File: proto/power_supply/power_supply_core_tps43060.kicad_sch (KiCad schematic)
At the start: 45 parts, among them Q201 TK4R3E06PL, Q202 TK4R3E06PL, U101 ZXCT1110, U202 TPS43060

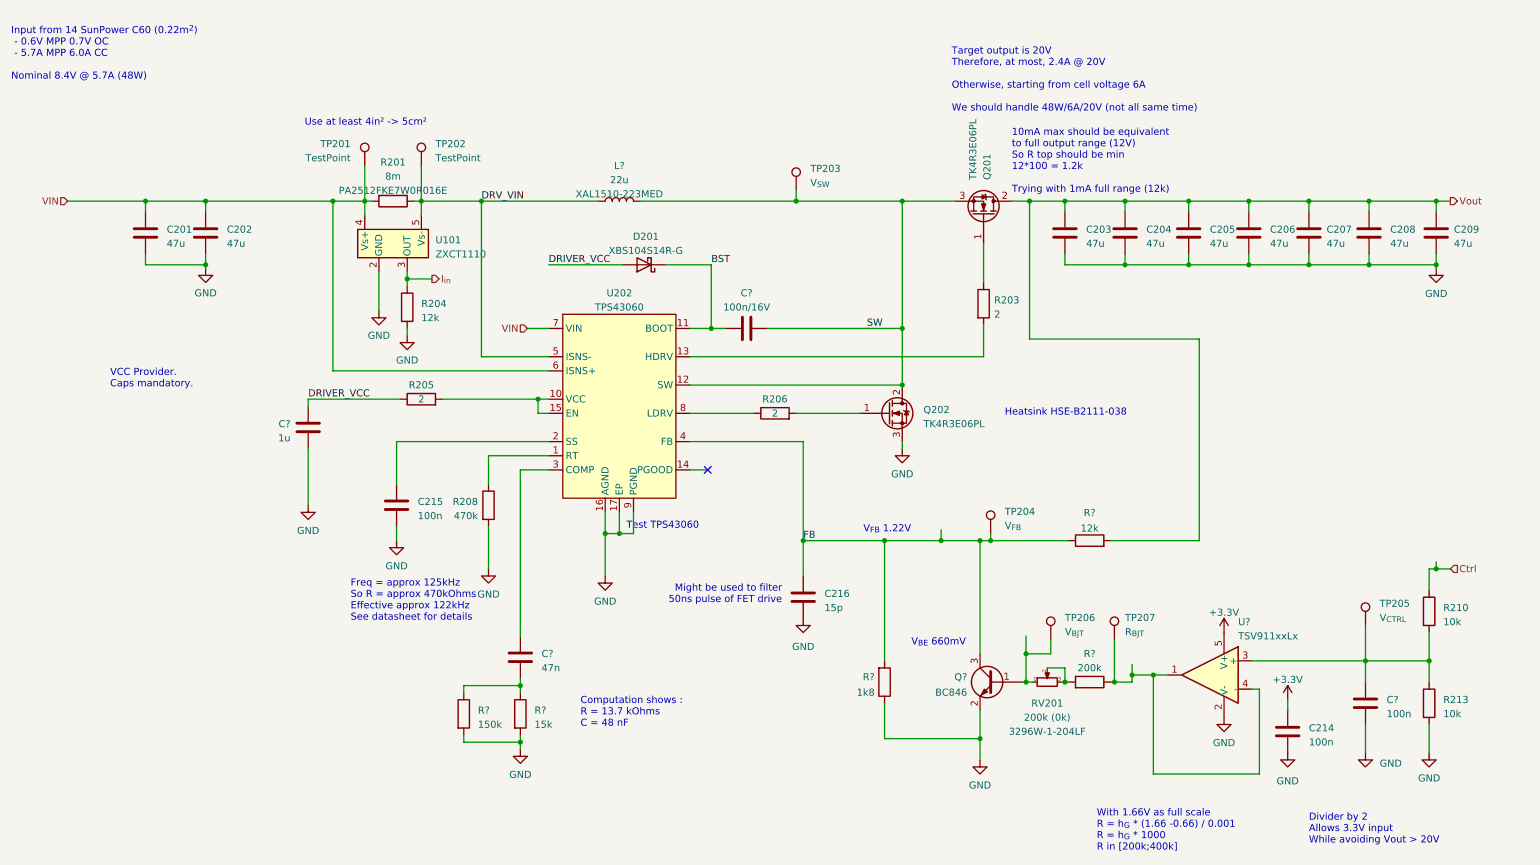
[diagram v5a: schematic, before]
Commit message: Update for BOM
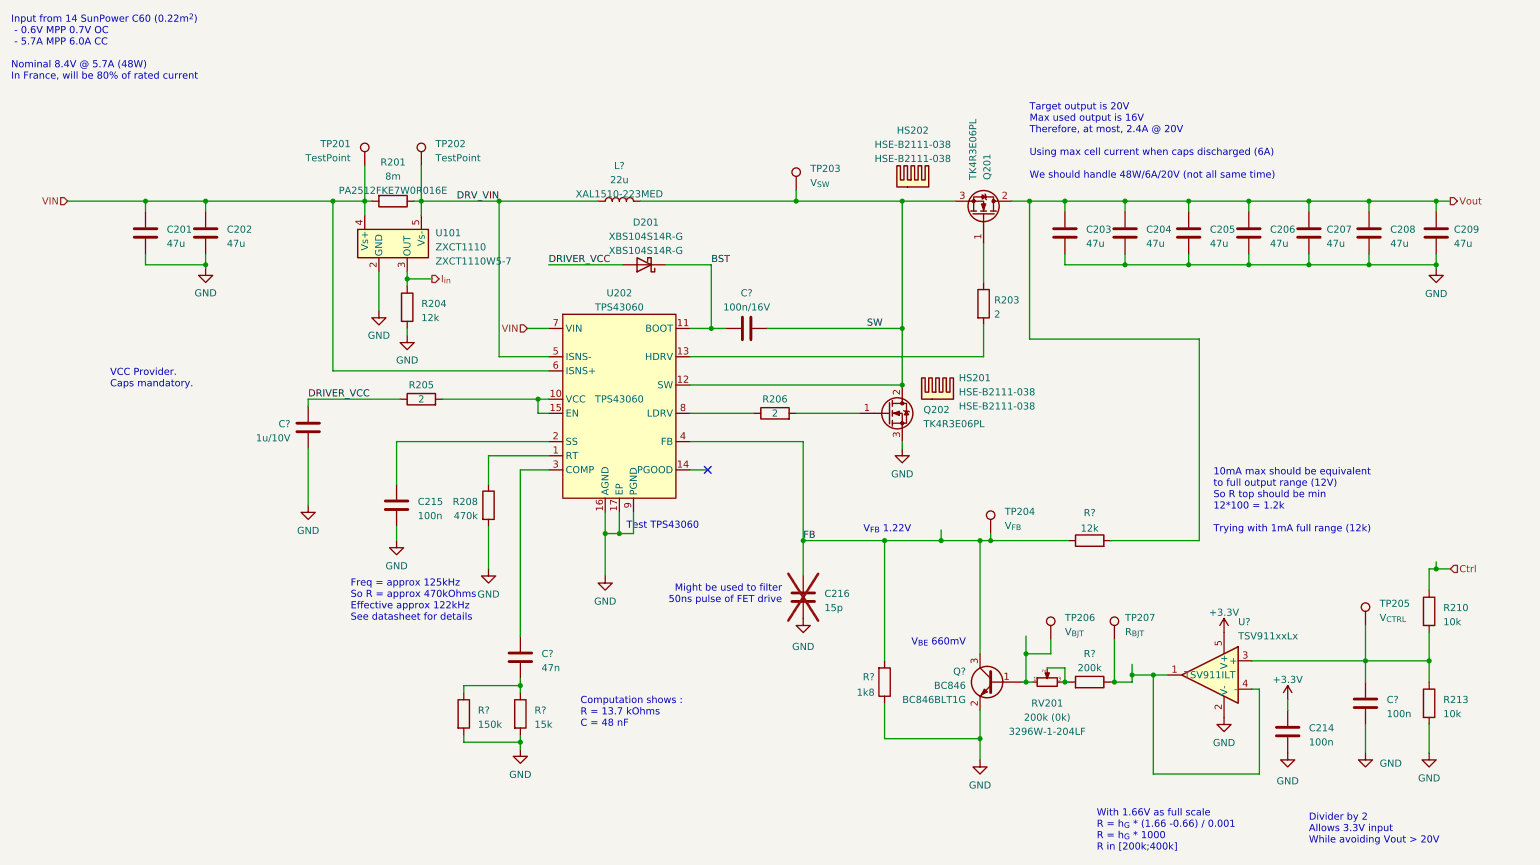
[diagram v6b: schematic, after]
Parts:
- added HS201, HS202: HSE-B2111-038, symbol Mechanical:Heatsink
- C216: now not fitted; now left out of the parts list
- C?: value 1u -> 1u/10V
- D201: MPN (none) -> XBS104S14R-G
- Q?: MPN (none) -> BC846BLT1G
- TP201, TP202, TP203, TP204, TP205, TP206, TP207: now left out of the parts list
- U101: MPN (none) -> ZXCT1110W5-7
- U202: MPN (none) -> TPS43060
- U?: MPN (none) -> TSV911ILT
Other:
- note added: "Input from 14 SunPower C60 (0.22m^{2}) - 0.6V MPP 0.7V OC - 5.7A MPP 6.0A CC Nominal 8.4V @ 5.7A (48W) In France, will be 80% of rated current"
- note added: "Target output is 20V Max used output is 16V Therefore, at most, 2.4A @ 20V Using max cell current when caps discharged (6A) We should handle 48W/6A/20V (not all same time)"
- note removed: "Heatsink HSE-B2111-038"
- note removed: "Input from 14 SunPower C60 (0.22m^{2}) - 0.6V MPP 0.7V OC - 5.7A MPP 6.0A CC Nominal 8.4V @ 5.7A (48W)"
- note removed: "Target output is 20V Therefore, at most, 2.4A @ 20V Otherwise, starting from cell voltage 6A We should handle 48W/6A/20V (not all same time)"
- note removed: "Use at least 4in² -> 5cm²"
- company: (none) -> Julien FAUCHER
- title: (none) -> MPPT PSU - Core boost converter

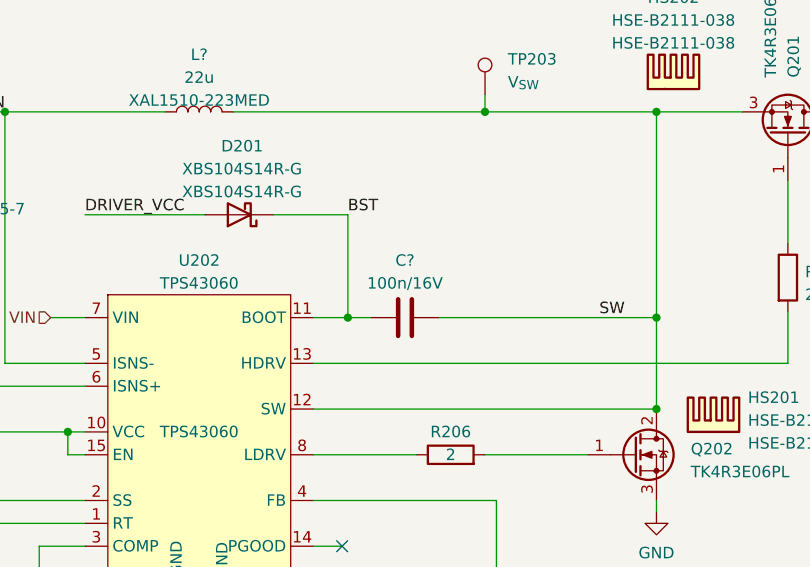
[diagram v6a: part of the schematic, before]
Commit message: [PCB] Elaborate BOM
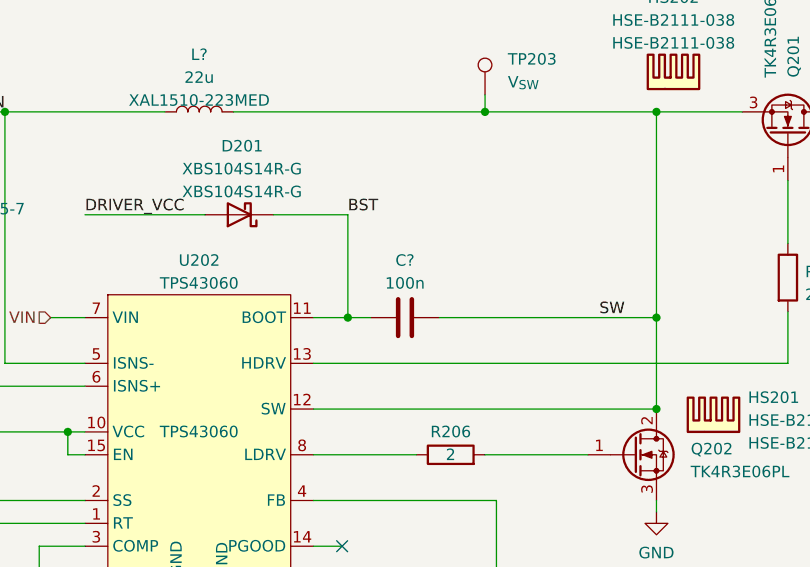
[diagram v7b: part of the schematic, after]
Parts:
- C201, C202, C203, C204, C205, C206, C207, C208, C209: MPN C2012X5R1V156M125AC -> C3216X5R1E476M160AC; Mouser SKU (none) -> 810-C3216X5R1E476M
- C214, C215, C?: MPN (none) -> 0805YC104M4T2A; Mouser SKU (none) -> 581-0805YC104M4T2A
- C?: value 100n/16V -> 100n; MPN (none) -> 0805YC104M4T2A; Mouser SKU (none) -> 581-0805YC104M4T2A; Notes (none) -> 16V
- D201: Mouser SKU (none) -> 865-XBS104S14R-G
- HS201, HS202: Mouser SKU (none) -> 490-HSE-B2111-038
- L?: Mouser SKU (none) -> 994-XAL1510-223MED
- Q201, Q202: Mouser SKU (none) -> 757-TK4R3E06PLS1X
- Q?: Mouser SKU (none) -> 863-BC846BLT1G
- R201: Mouser SKU (none) -> 603-PA2512FKE7W0R16E
- R203, R205, R206: MPN (none) -> CHP0805QFW-2R00ELF; Mouser SKU (none) -> 652-CHP0805QFW-2R00ELF
- RV201: Mouser SKU (none) -> 652-3296W-1-204LF
- U101: Mouser SKU (none) -> 522-ZXCT1110W5-7
- U202: Mouser SKU (none) -> 595-TPS43060RTER
- U?: Mouser SKU (none) -> 511-TSV911ILT
